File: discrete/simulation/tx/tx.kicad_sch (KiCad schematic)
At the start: 28 parts, among them Q1 2N3904, Q2 2N3906, Q3 2N3904, Q4 2N3906, Q5 2N3904, Q6 2N3906

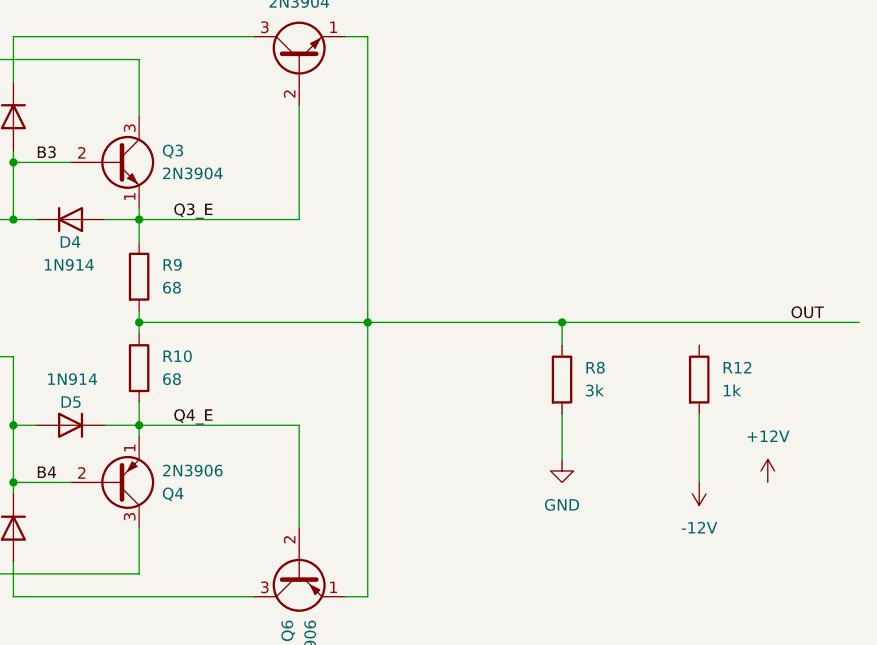
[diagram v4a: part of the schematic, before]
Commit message: Switch to better suited current limiting transistors for the transmitter. Validate 2N5551 and 2N5401 SPICE models in transmitter
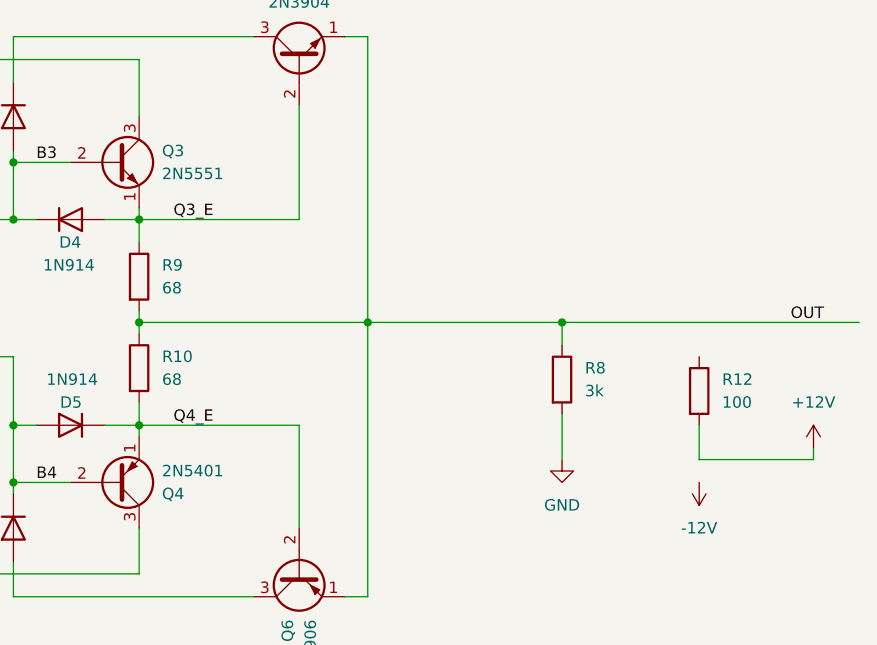
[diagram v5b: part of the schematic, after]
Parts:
- Q3: value 2N3904 -> 2N5551
- Q4: value 2N3906 -> 2N5401
- R12: value 1k -> 100
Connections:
- net +12V: now also R12.2
- net -12V: no longer R12.2
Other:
- moved on the sheet: R12
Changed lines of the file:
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@@
 	(wire
 		(pts
-			(xy 173.99 74.93) (xy 199.39 74.93)
+			(xy 248.92 90.17) (xy 236.22 90.17)
 		)
 		(stroke
@@
 	(wire
 		(pts
-			(xy 68.58 43.18) (xy 68.58 45.72)
+			(xy 173.99 74.93) (xy 199.39 74.93)
 		)
 		(stroke
@@
 	(wire
 		(pts
-			(xy 113.03 71.12) (xy 120.65 71.12)
+			(xy 68.58 43.18) (xy 68.58 45.72)
 		)
 		(stroke
@@
 	(wire
 		(pts
-			(xy 38.1 157.48) (xy 50.8 157.48)
+			(xy 113.03 71.12) (xy 120.65 71.12)
 		)
 		(stroke
@@
 	(wire
 		(pts
-			(xy 68.58 45.72) (xy 68.58 59.69)
+			(xy 38.1 157.48) (xy 50.8 157.48)
 		)
 		(stroke
@@
 	(wire
 		(pts
-			(xy 173.99 102.87) (xy 128.27 102.87)
+			(xy 68.58 45.72) (xy 68.58 59.69)
 		)
 		(stroke
@@
 	(wire
 		(pts
-			(xy 236.22 85.09) (xy 236.22 92.71)
+			(xy 173.99 102.87) (xy 128.27 102.87)
 		)
 		(stroke
@@
 	(wire
 		(pts
+			(xy 248.92 88.9) (xy 248.92 90.17)
+		)
+		(stroke
+			(width 0)
+			(type default)
+		)
+	)
+	(wire
+		(pts
+			(xy 236.22 90.17) (xy 236.22 86.36)
+		)
+		(stroke
+			(width 0)
+			(type default)
+		)
+	)
+	(wire
+		(pts
 			(xy 93.98 71.12) (xy 101.6 71.12)
 		)
@@
 			)
 		)
-		(property "Value" "2N3904"
+		(property "Value" "2N5551"
 			(at 176.53 58.4199 0)
 			(effects
@@
 			)
 		)
-		(property "Sim.Type" "VBIC"
+		(property "Sim.Type" "GUMMELPOON"
+			(at 171.45 57.15 0)
+			(effects
+				(font
+					(size 1.27 1.27)
+				)
+				(hide yes)
+			)
+		)
+		(property "Sim.Library" "/home/sfinneran/work/ACMS/PDP-8-Serial/discrete/simulation/models/tx_output_ngspice.lib"
+			(at 171.45 57.15 0)
+			(effects
+				(font
+					(size 1.27 1.27)
+				)
+				(hide yes)
+			)
+		)
+		(property "Sim.Name" "2N5551"
 			(at 171.45 57.15 0)
 			(effects
@@
 	(symbol
 		(lib_id "Device:R")
-		(at 236.22 81.28 0)
+		(at 236.22 82.55 0)
 		(unit 1)
 		(exclude_from_sim no)
@@
 		(fields_autoplaced yes)
 		(property "Reference" "R12"
-			(at 238.76 80.0099 0)
+			(at 238.76 81.2799 0)
 			(effects
 				(font
@@
 			)
 		)
-		(property "Value" "1k"
-			(at 238.76 82.5499 0)
+		(property "Value" "100"
+			(at 238.76 83.8199 0)
 			(effects
 				(font
@@
 		)
 		(property "Footprint" ""
-			(at 234.442 81.28 90)
+			(at 234.442 82.55 90)
 			(effects
 				(font
@@
 		)
 		(property "Datasheet" "~"
-			(at 236.22 81.28 0)
+			(at 236.22 82.55 0)
 			(effects
 				(font
@@
 		)
 		(property "Description" "Resistor"
-			(at 236.22 81.28 0)
+			(at 236.22 82.55 0)
 			(effects
 				(font
@@
 			)
 		)
-		(property "Value" "2N3906"
+		(property "Value" "2N5401"
 			(at 176.53 91.4401 0)
 			(effects
@@
 			)
 		)
-		(property "Sim.Type" "VBIC"
+		(property "Sim.Type" "GUMMELPOON"
+			(at 171.45 92.71 0)
+			(effects
+				(font
+					(size 1.27 1.27)
+				)
+				(hide yes)
+			)
+		)
+		(property "Sim.Library" "/home/sfinneran/work/ACMS/PDP-8-Serial/discrete/simulation/models/tx_output_ngspice.lib"
+			(at 171.45 92.71 0)
+			(effects
+				(font
+					(size 1.27 1.27)
+				)
+				(hide yes)
+			)
+		)
+		(property "Sim.Name" "2N5401"
 			(at 171.45 92.71 0)
 			(effects
@@
 	(symbol
 		(lib_id "power:+10V")
-		(at 243.84 92.71 0)
+		(at 248.92 88.9 0)
 		(unit 1)
 		(exclude_from_sim no)
@@
 		(fields_autoplaced yes)
 		(property "Reference" "#PWR011"
-			(at 243.84 96.52 0)
+			(at 248.92 92.71 0)
 			(effects
 				(font
@@
 		)
 		(property "Value" "+12V"
-			(at 243.84 87.63 0)
+			(at 248.92 83.82 0)
 			(effects
 				(font
@@
 		)
 		(property "Footprint" ""
-			(at 243.84 92.71 0)
+			(at 248.92 88.9 0)
 			(effects
 				(font
@@
 		)
 		(property "Datasheet" ""
-			(at 243.84 92.71 0)
+			(at 248.92 88.9 0)
 			(effects
 				(font
@@
 		)
 		(property "Description" "Power symbol creates a global label with name \"+10V\""
-			(at 243.84 92.71 0)
+			(at 248.92 88.9 0)
 			(effects
 				(font

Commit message: Validate discrete RS232 transmitter with final transistor models
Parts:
- added Q10, Q8: 2N3906, Package_TO_SOT_THT:TO-92_Inline, symbol Transistor_BJT:2N3906
- added Q7, Q9: 2N3904, Package_TO_SOT_THT:TO-92_Inline, symbol Transistor_BJT:2N3904
- Q1, Q5: value 2N3904 -> 2N5551
- Q2, Q6: value 2N3906 -> 2N5401
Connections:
- net OUT: now also R12.1

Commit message: Update to match W050 open collector output drives. Updated design simulation
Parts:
- removed Q10, Q8: 2N3906, Package_TO_SOT_THT:TO-92_Inline, symbol Transistor_BJT:2N3906
- removed Q7, Q9: 2N3904, Package_TO_SOT_THT:TO-92_Inline, symbol Transistor_BJT:2N3904
- added DW1, DW2: 1N914, Diode_THT:D_DO-35_SOD27_P7.62mm_Horizontal, symbol Diode:1N914
- added I1: 90m, symbol Simulation_SPICE:IDC
- added QW1, QW2: 2N5401, Package_TO_SOT_THT:TO-92_Inline, symbol Transistor_BJT:2N3906
- added RW1: 1k8, symbol Device:R
- added RW2: 15k, symbol Device:R
- added RW3: 7k5, symbol Device:R
- added RW4: 47k, symbol Device:R
- added RW5: 100k, symbol Device:R
- added RW6: 10k, symbol Device:R
- R2: value 180k -> 47k
- V1: value 10 -> 9.5
- V2: value 15 -> 16.5
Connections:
- net +10V: now also RW5.2
- net +12V: no longer R12.2
- net -15V: now also I1.2, RW2.1, RW3.1, RW6.2
- net GND: now also DW1.2 (A), DW2.1 (K), QW2.1 (E)
- net TTO: now also QW1.3 (C), RW3.2, RW4.1; no longer R1.1, V3.1
- new net: DW1.1 (K), I1.1, QW1.1 (E)
- new net: DW2.2 (A), QW2.2 (B), RW4.2, RW5.1
- new net: QW1.2 (B), RW1.2
- new net TTO_INV: QW2.3 (C), R1.1, RW6.1
- new net W050_IN: RW1.1, RW2.2, V3.1
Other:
- note added: "+10V"
- note added: "15V"
- moved on the sheet: D1, D2, D3, D4, D5, Q1, Q2, Q3, Q4, Q5, Q6, R1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
